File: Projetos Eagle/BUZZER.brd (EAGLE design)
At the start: 39.8 x 21.5 mm, 8 parts, among them J1 CONECTOR_IN, J2 CONECTOR, Q1 BC817, U1 74HC132

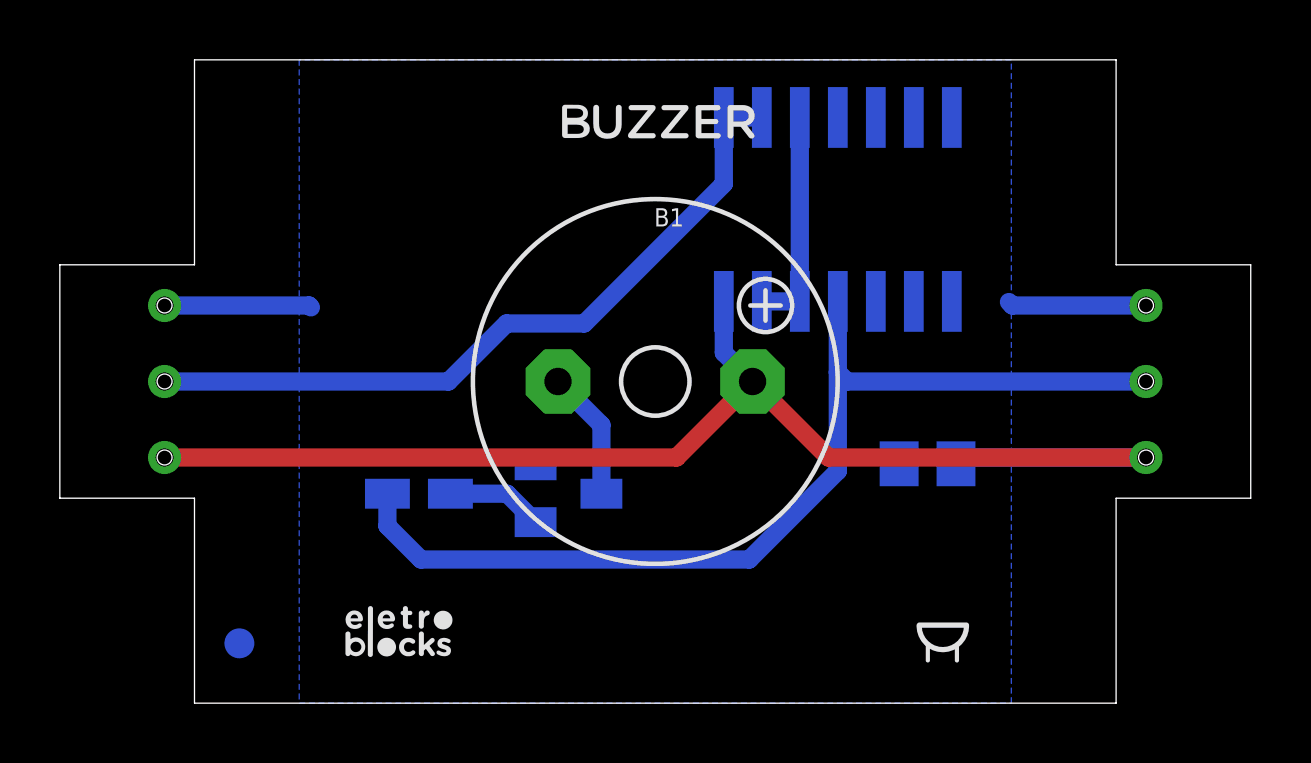
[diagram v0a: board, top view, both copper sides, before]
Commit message: correção de pads e adição de label para versionamento
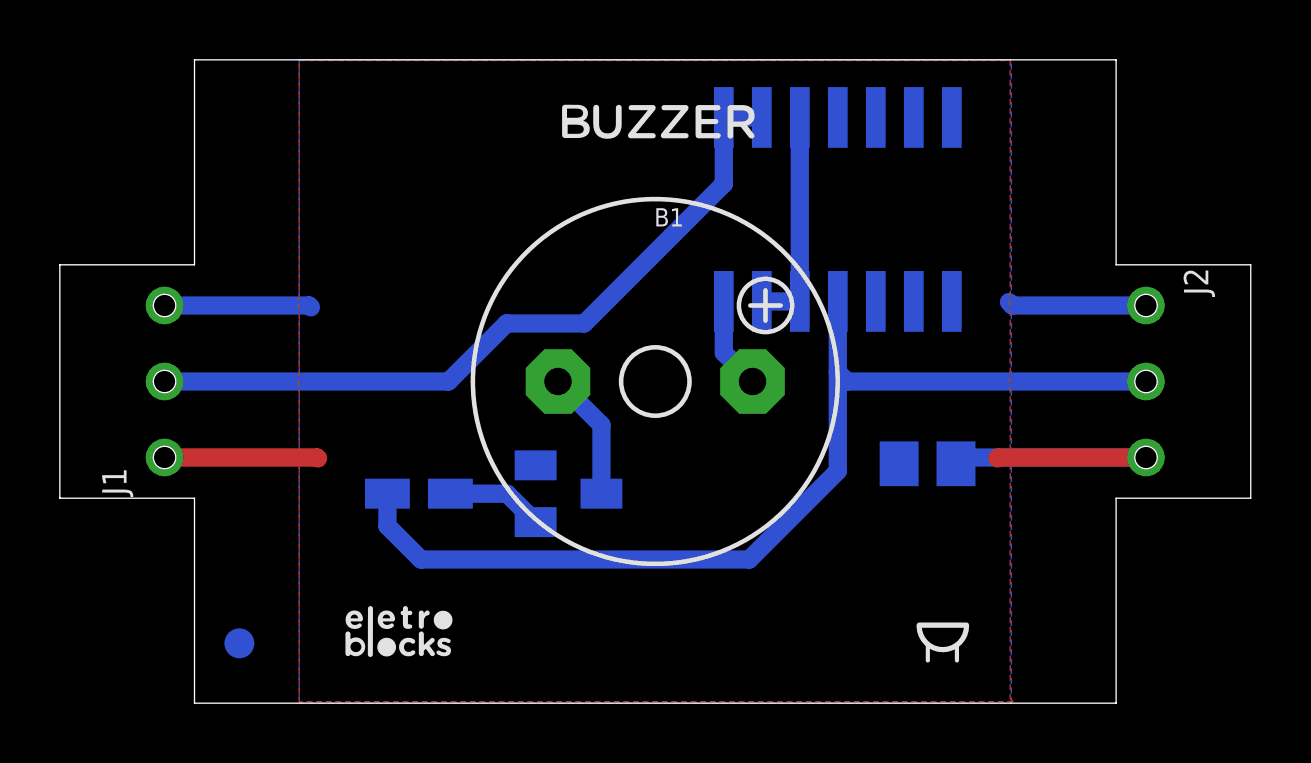
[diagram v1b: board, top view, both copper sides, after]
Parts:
- J1: value CONECTOR_IN -> CONECTOR_MACHO
- J2: value CONECTOR -> CONECTOR_FEMEA
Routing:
- net VCC: track 44.4 -> 19.6 mm
- added copper zone on layer 1, net VCC
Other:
- board text added: "V1.0.1"
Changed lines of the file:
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@@
 <drawing>
 <settings>
-<setting alwaysvectorfont="no"/>
+<setting alwaysvectorfont="yes"/>
 <setting verticaltext="up"/>
 </settings>
@@
 <vertex x="21.96633125" y="1.36031875"/>
 </polygon>
+<text x="-0.45" y="21.5" size="0.6096" layer="26" font="vector" rot="MR270">V1.0.1</text>
 </plain>
 <attributes>
@@
 <attribute name="VALUE" x="23.16" y="6.95" size="0.6096" layer="28" font="fixed" rot="MR90"/>
 </element>
-<element name="J1" library="Eletroblocks Lib" package="3CONECTOR" override_package3d_urn="urn:adsk.eagle:package:22321382/3" override_package_urn="urn:adsk.eagle:footprint:22321383/1" value="CONECTOR_IN" x="-4.5" y="10.75" smashed="yes"/>
-<element name="J2" library="Eletroblocks Lib" package="3CONECTOR" override_package3d_urn="urn:adsk.eagle:package:22308003/4" override_package_urn="urn:adsk.eagle:footprint:22308004/1" value="CONECTOR" x="28.3" y="10.75" smashed="yes" rot="R180"/>
+<element name="J1" library="Eletroblocks Lib" package="3CONECTOR" override_package3d_urn="urn:adsk.eagle:package:22321382/3" override_package_urn="urn:adsk.eagle:footprint:22321383/1" override_locally_modified="yes" value="CONECTOR_MACHO" x="-4.5" y="10.75" smashed="yes">
+<attribute name="NAME" x="-5.77" y="6.94" size="0.8128" layer="21" font="fixed" rot="R90"/>
+</element>
+<element name="J2" library="Eletroblocks Lib" package="3CONECTOR" override_package3d_urn="urn:adsk.eagle:package:22308003/4" override_package_urn="urn:adsk.eagle:footprint:22308004/1" override_locally_modified="yes" value="CONECTOR_FEMEA" x="28.3" y="10.75" smashed="yes" rot="R180">
+<attribute name="NAME" x="29.57" y="14.56" size="0.8128" layer="21" font="fixed" rot="R270"/>
+</element>
 <element name="Q1" library="semicon-smd-ipc" library_urn="urn:adsk.eagle:library:353" package="SOT23" package3d_urn="urn:adsk.eagle:package:28738/2" value="BC817" x="9" y="7" smashed="yes" rot="MR90">
-<attribute name="NAME" x="9.90931875" y="5.770640625" size="0.6096" layer="26" font="fixed" rot="MR90"/>
+<attribute name="NAME" x="9.86931875" y="5.470640625" size="0.6096" layer="26" font="fixed" rot="MR90"/>
 <attribute name="POPULARITY" value="0" x="13.69391875" y="-4.948159375" size="1.778" layer="28" rot="MR90" display="off"/>
 <attribute name="VALUE" x="5.825" y="5.095" size="1.27" layer="28" rot="MR90"/>
@@
 <contactref element="U1" pad="14"/>
 <contactref element="B1" pad="+"/>
-<wire x1="28.3" y1="8.21" x2="17.6912" y2="8.21" width="0.6096" layer="1"/>
-<wire x1="17.6912" y1="8.21" x2="15.1512" y2="10.75" width="0.6096" layer="1"/>
-<wire x1="12.6112" y1="8.21" x2="15.1512" y2="10.75" width="0.6096" layer="1"/>
-<wire x1="-4.5" y1="8.21" x2="12.6112" y2="8.21" width="0.6096" layer="1"/>
 <wire x1="14.19" y1="13.4266" x2="14.19" y2="11.7112" width="0.6096" layer="16"/>
 <wire x1="14.19" y1="11.7112" x2="15.1512" y2="10.75" width="0.6096" layer="16"/>
+<polygon width="0.1524" layer="1">
+<vertex x="0" y="0"/>
+<vertex x="0" y="21.48"/>
+<vertex x="23.76" y="21.48"/>
+<vertex x="23.76" y="0.15"/>
+<vertex x="23.86" y="0.05"/>
+<vertex x="0.05" y="0.05"/>
+</polygon>
+<wire x1="-4.5" y1="8.21" x2="0.6" y2="8.21" width="0.6096" layer="1"/>
+<wire x1="0.6" y1="8.21" x2="0.63" y2="8.18" width="0.6096" layer="1"/>
+<wire x1="28.3" y1="8.21" x2="23.36" y2="8.21" width="0.6096" layer="1"/>
+<wire x1="23.36" y1="8.21" x2="23.33" y2="8.18" width="0.6096" layer="1"/>
 </signal>
 <signal name="SIGNAL_IN">
